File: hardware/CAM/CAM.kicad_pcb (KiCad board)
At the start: 2 copper layers, 40 x 40 mm, 17 parts, among them J1 Input, U1 AS5047P, U2 AMS1117-5.0

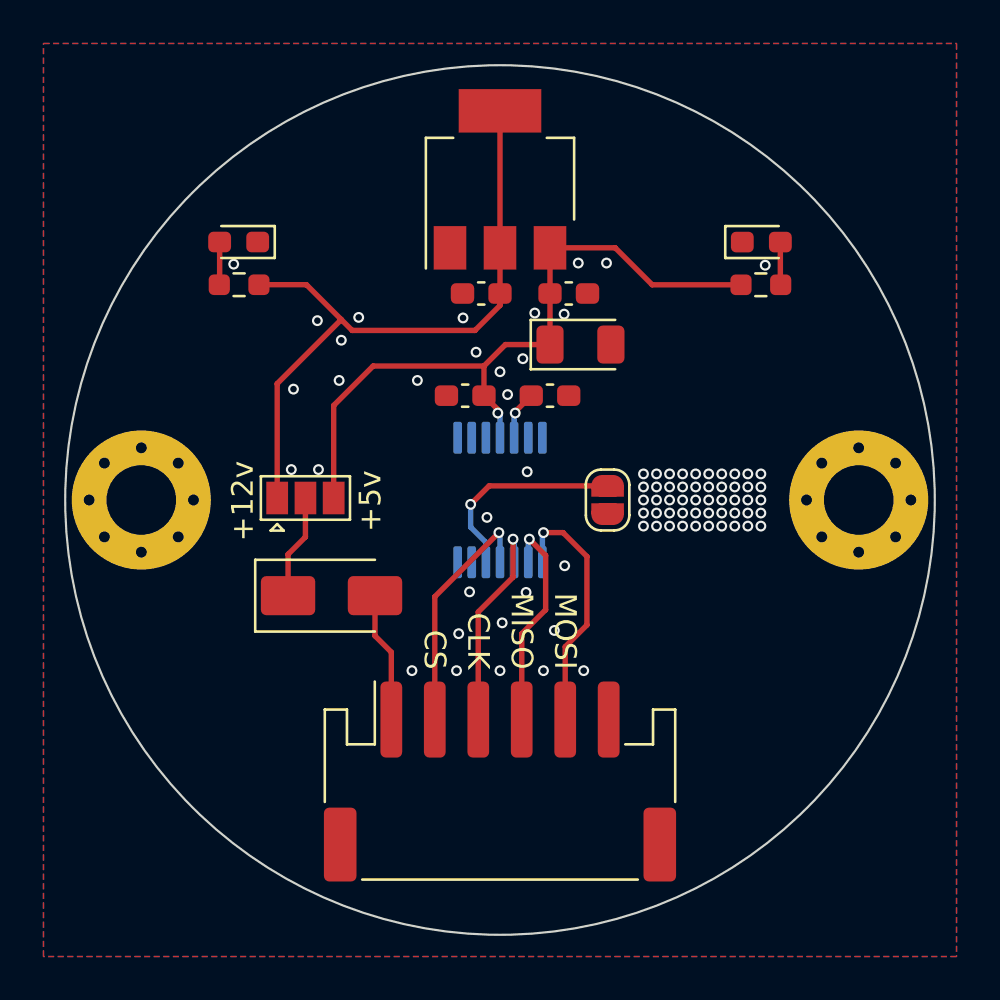
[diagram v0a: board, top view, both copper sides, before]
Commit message: simplify camshaft sensor schematic and add extra mounting hole
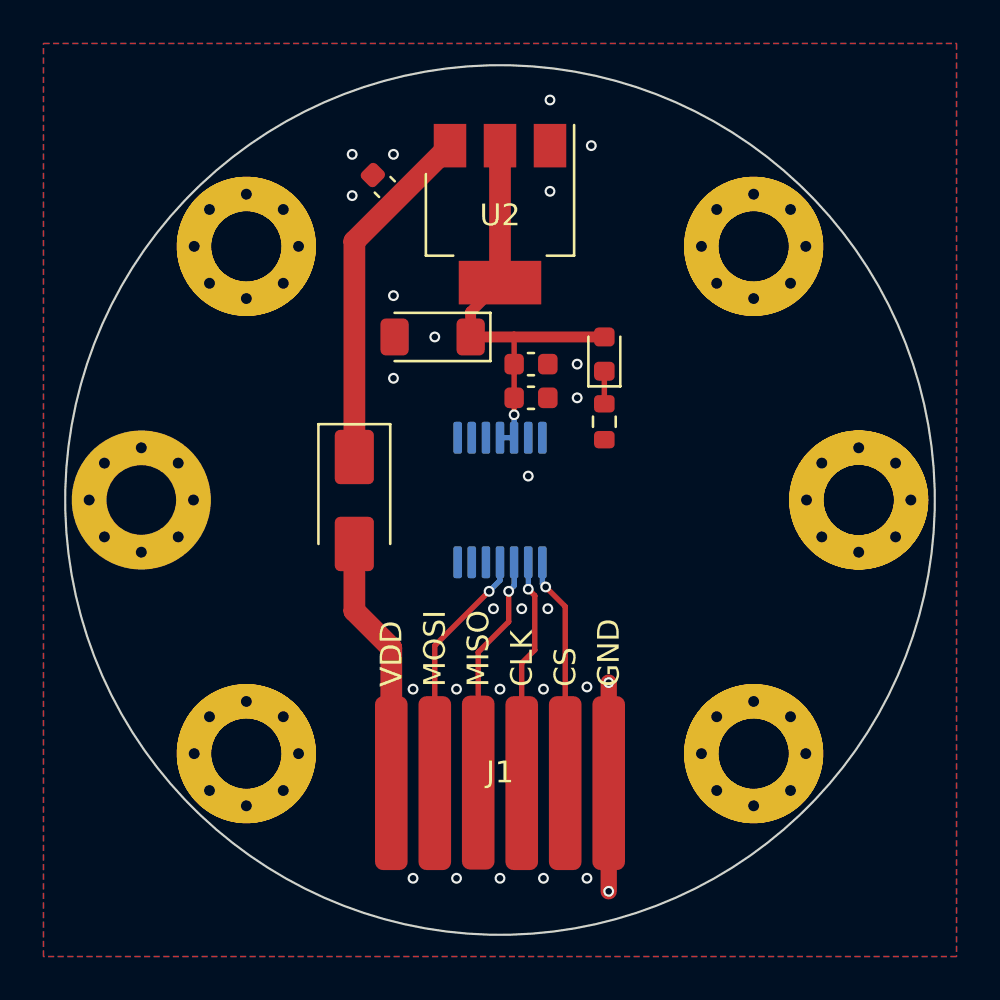
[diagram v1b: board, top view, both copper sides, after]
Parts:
- removed C4: 0.33uf, Capacitor_SMD:C_0603_1608Metric_Pad1.08x0.95mm_HandSolder
- removed D4: 1n4001, Diode_SMD:D_SMA
- removed JP1: ~, Jumper:SolderJumper-2_P1.3mm_Open_RoundedPad1.0x1.5mm
- removed JP2: 5V/12V, Jumper:SolderJumper-3_P1.3mm_Open_Pad1.0x1.5mm
- removed R2: 680, Resistor_SMD:R_0603_1608Metric_Pad0.98x0.95mm_HandSolder
- added ?: , , F.Cu at (161.7, 71.7)
- added ?: , , F.Cu at (138.3, 71.7)
- added ?: , , F.Cu at (166.5, 60.0)
- added ?: , , F.Cu at (161.7, 48.3)
- added ?: , , F.Cu at (138.3, 48.3)
- added REF**: MountingHole_3.2mm_M3_Pad_Via, MountingHole:MountingHole_3.2mm_M3_Pad_Via, F.Cu at (138.3, 48.3)
- added REF**: MountingHole_3.2mm_M3_Pad_Via, MountingHole:MountingHole_3.2mm_M3_Pad_Via, F.Cu at (161.7, 48.3)
- added REF**: MountingHole_3.2mm_M3_Pad_Via, MountingHole:MountingHole_3.2mm_M3_Pad_Via, F.Cu at (161.7, 71.7)
- added REF**: MountingHole_3.2mm_M3_Pad_Via, MountingHole:MountingHole_3.2mm_M3_Pad_Via, F.Cu at (138.3, 71.7)
- C1: value 100nf -> 100n; footprint Capacitor_SMD:C_0603_1608Metric_Pad1.08x0.95mm_HandSolder -> Capacitor_SMD:C_0603_1608Metric
- C2: value 1uf -> 100n; footprint Capacitor_SMD:C_0603_1608Metric_Pad1.08x0.95mm_HandSolder -> Capacitor_SMD:C_0603_1608Metric
- C3: value 100nf -> 330n; footprint Capacitor_SMD:C_0603_1608Metric_Pad1.08x0.95mm_HandSolder -> Capacitor_SMD:C_0603_1608Metric
- D1: value LED -> 1n4001; footprint LED_SMD:LED_0603_1608Metric_Pad1.05x0.95mm_HandSolder -> Diode_SMD:D_SMA
- D2: value LED -> 3.6v; footprint LED_SMD:LED_0603_1608Metric_Pad1.05x0.95mm_HandSolder -> Diode_SMD:D_MiniMELF
- D3: value 5.1v -> LED; footprint Diode_SMD:D_1206_3216Metric -> Diode_SMD:D_0603_1608Metric
- J1: footprint Connector_JST:JST_PH_S6B-PH-SM4-TB_1x06-1MP_P2.00mm_Horizontal -> My_Lirbrary:6P_Board_To_Wire_Pad
- R1: value 220 -> 680; footprint Resistor_SMD:R_0603_1608Metric_Pad0.98x0.95mm_HandSolder -> Resistor_SMD:R_0603_1608Metric
- U2: value AMS1117-5.0 -> AMS1117-3.3
- moved D1 22.2 mm to (143.3, 60.0), turned to -90 degrees
- moved D2 9.93 mm to (146.9, 52.5)
- moved C3 9.78 mm to (144.7, 45.6), turned to 135 degrees
- moved R1 9.57 mm to (154.8, 56.4), turned to -90 degrees
- moved C1 3.03 mm to (151.4, 55.3), turned to 0 degrees
- moved C2 1.69 mm to (151.4, 53.8), turned to 0 degrees
- moved U2 1.60 mm to (150.0, 46.9), turned to -90 degrees
- moved D3 1.18 mm to (154.8, 53.3), turned to 90 degrees
- moved J1 0.07 mm to (150.0, 73.0)
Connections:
- C1 pad 1: Net-(D3-K) -> +3V3
- C2 pad 1: GND -> +3V3
- C2 pad 2: Net-(U1-VDD3V3) -> GND
- C3 pad 1: Net-(D3-K) -> Net-(D1-K)
- D1 pad 1: GND -> Net-(D1-K)
- D1 pad 2: Net-(D1-A) -> VDD
- D2 pad 1: GND -> +3V3
- D2 pad 2: Net-(D2-A) -> GND
- D3 pad 2: GND -> +3V3
- R1 pad 2: Net-(D1-A) -> GND
- U1 pad 11: Net-(D3-K) -> +3V3
- U1 pad 12: Net-(U1-VDD3V3) -> +3V3
- U1 pad 5: Net-(JP1-B) -> unconnected-(U1-TST-Pad5)
- U2 pad 2: Net-(JP2-A) -> +3V3
- U2 pad 3: Net-(D3-K) -> Net-(D1-K)
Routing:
- net Net-(D3-K): track 32.9 -> 1.50 mm, vias 1 -> 0
- net Net-(JP2-A): track 30.8 -> 0.00 mm
- net +3V3: track 0.00 -> 20.8 mm, vias 0 -> 1
- net Net-(D1-K): track 0.00 -> 16.1 mm
- net Net-(JP1-B): track 9.60 -> 0.00 mm, vias 1 -> 0
- net GND: track 0.01 -> 9.60 mm, vias 82 -> 27
- net VDD: track 6.01 -> 11.7 mm
- net Net-(D4-K): track 4.82 -> 0.00 mm
- net Net-(U1-VDD3V3): track 2.26 -> 0.00 mm, vias 1 -> 0
- net Net-(D2-A): track 1.97 -> 0.00 mm
- net Net-(D1-A): track 1.97 -> 0.00 mm
- net /CS: track 11.8 -> 10.6 mm
- net /MISO: track 10.0 -> 10.8 mm
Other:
- board text added: "Camshaft Sensor V1 Author: Collyn Power"
- board text added: "GND"
- board text added: "VDD"
- board text removed: "+12v"
- board text removed: "+5v"
- board text removed: "Cam Sensor V1.2"
